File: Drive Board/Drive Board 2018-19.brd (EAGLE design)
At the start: 379.8 x 115 mm, 113 parts, among them IC1 ACS758KCB, IC2 ACS758KCB, IC3 ACS758KCB, IC4 ACS758KCB, IC5 7812T, IC6 LM741P, K1 G5L, K2 G5L, K3 G5L

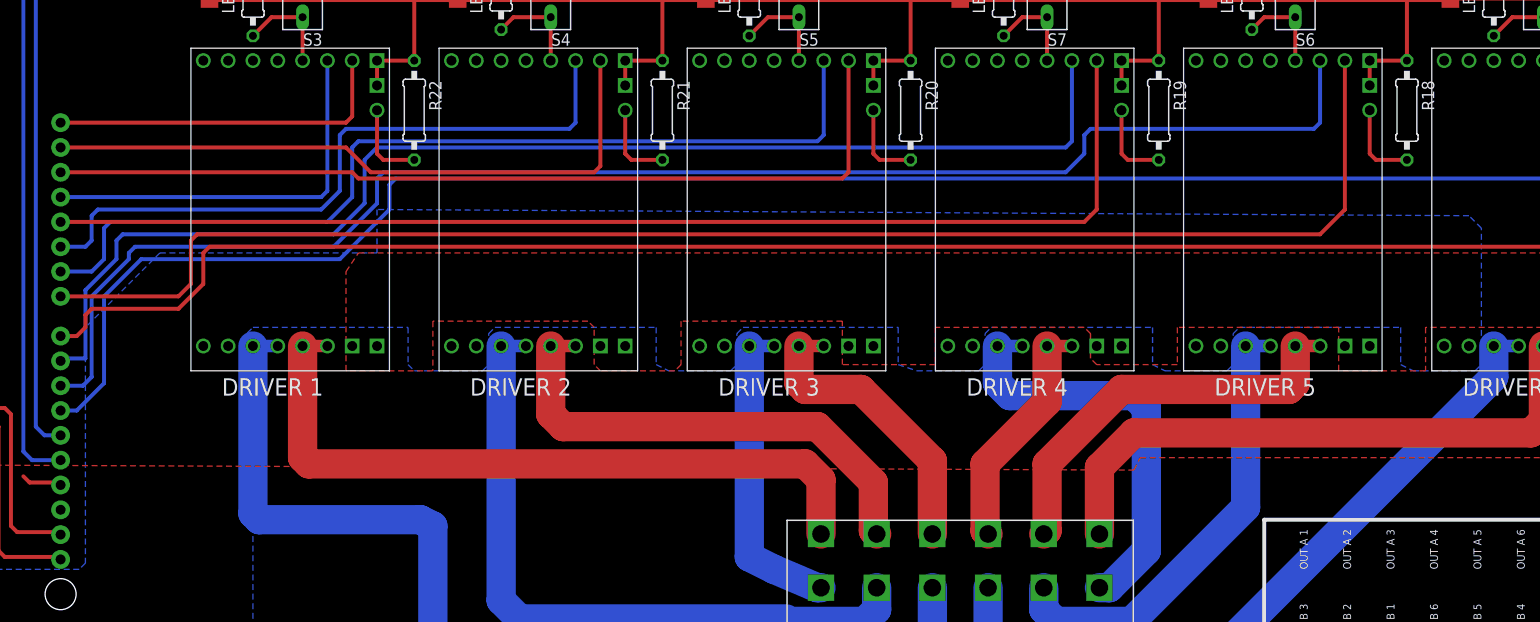
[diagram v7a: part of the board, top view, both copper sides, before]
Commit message: Updated Vin plane
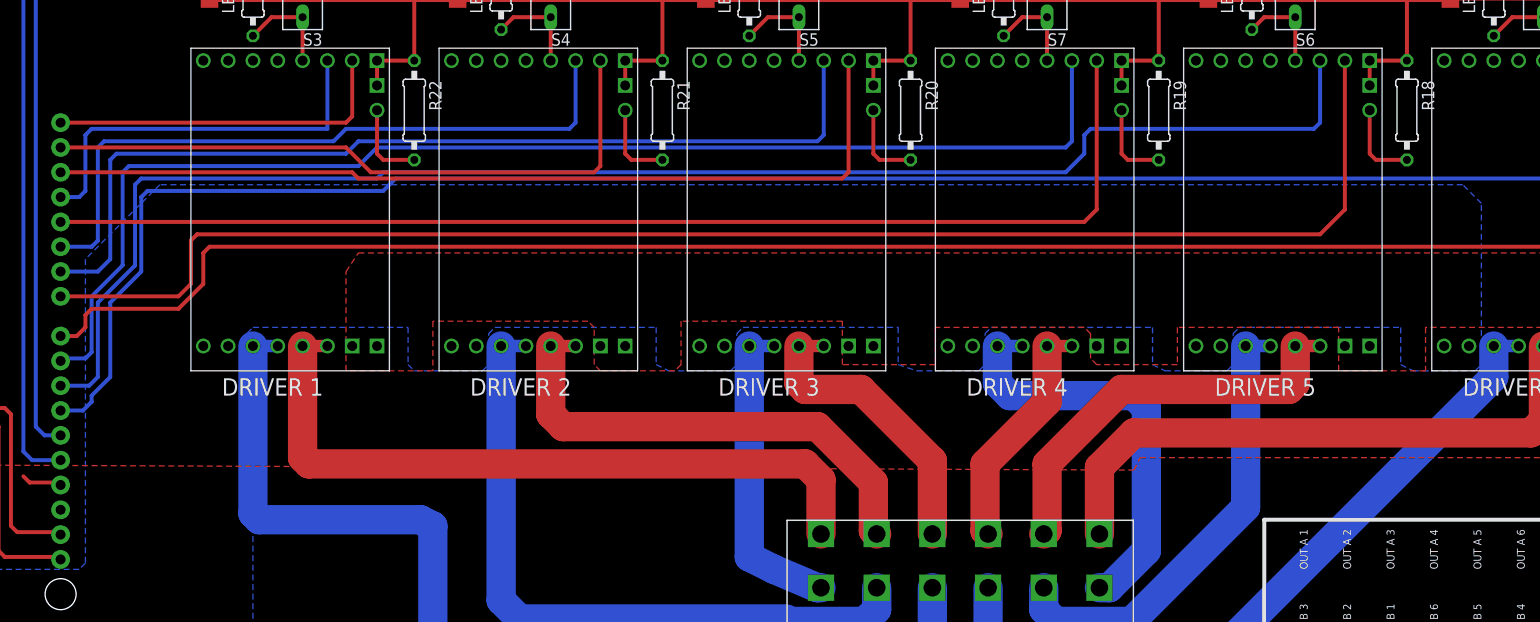
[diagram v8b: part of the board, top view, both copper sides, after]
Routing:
- net D11: track 182.5 -> 185.1 mm
- net D10: track 154.2 -> 156.8 mm
- net D9: track 128.9 -> 130.0 mm
- net D6: track 96.3 -> 97.5 mm
- net D5: track 69.2 -> 69.9 mm
